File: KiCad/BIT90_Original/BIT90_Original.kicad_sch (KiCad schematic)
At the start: 0 parts

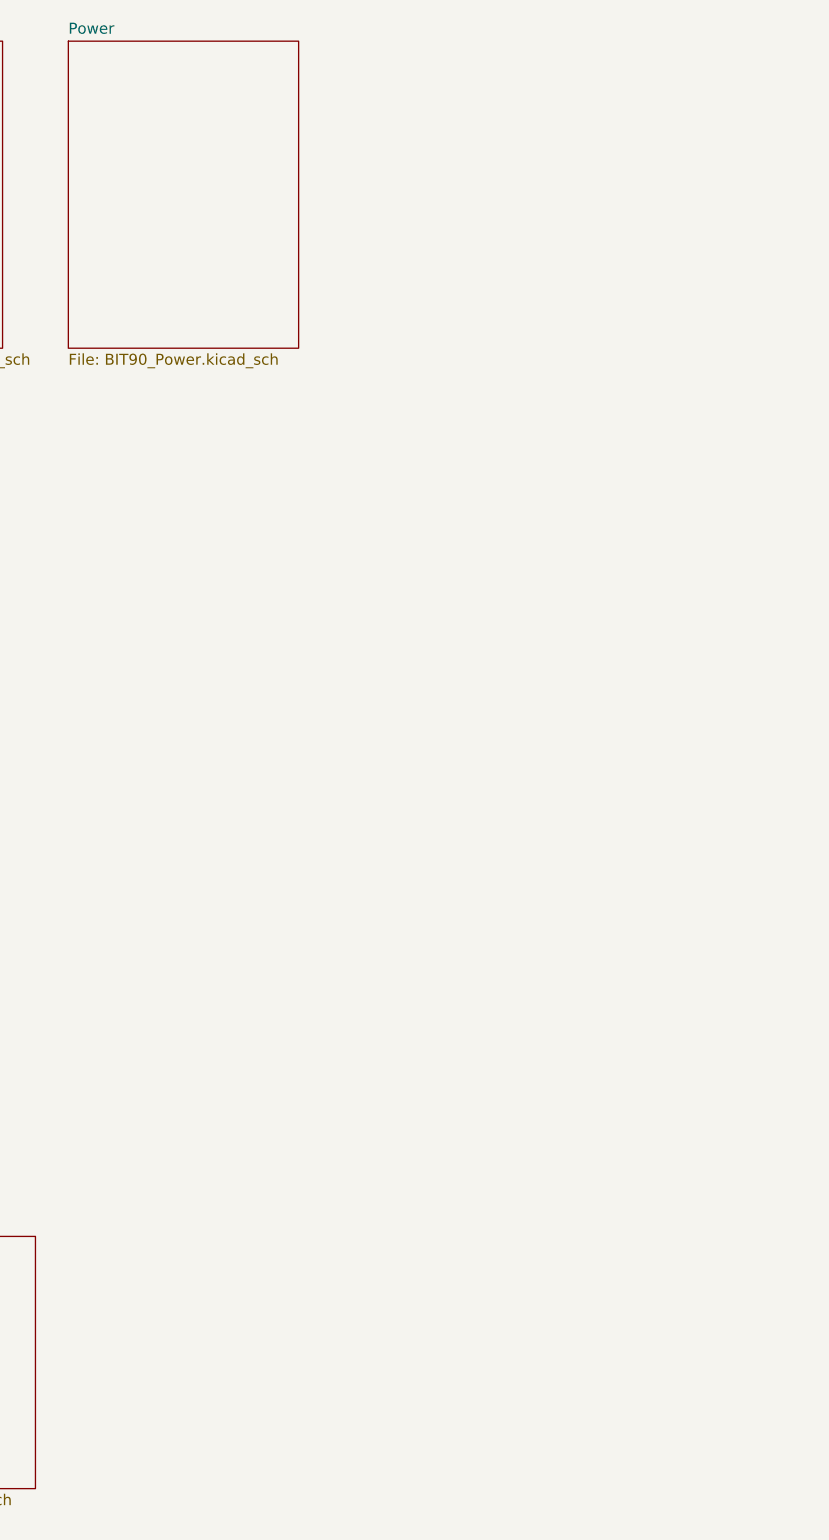
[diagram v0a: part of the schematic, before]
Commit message: Added "Processor" Sheet 6-1
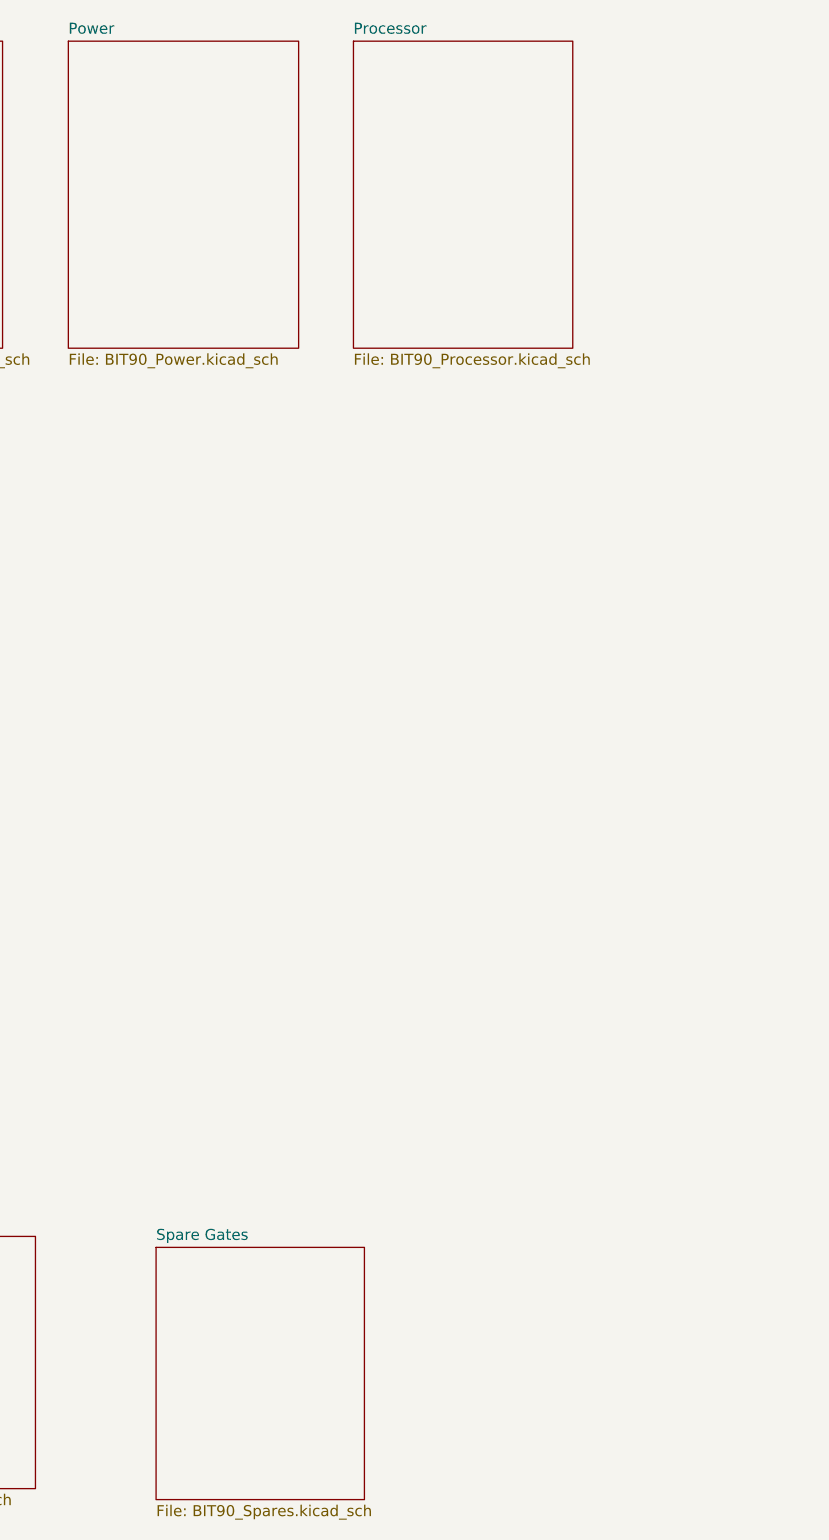
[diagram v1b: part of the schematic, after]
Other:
- added sheet Processor (BIT90_Processor.kicad_sch)
- added sheet Spare Gates (BIT90_Spares.kicad_sch)
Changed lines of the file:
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@@
+	)
+	(sheet
+		(at 88.9 21.59)
+		(size 25.4 35.56)
+		(exclude_from_sim no)
+		(in_bom yes)
+		(on_board yes)
+		(dnp no)
+		(fields_autoplaced yes)
+		(stroke
+			(width 0.1524)
+			(type solid)
+		)
+		(fill
+			(color 0 0 0 0.0000)
+		)
+		(property "Sheetname" "Processor"
+			(at 88.9 20.8784 0)
+			(effects
+				(font
+					(size 1.27 1.27)
+				)
+				(justify left bottom)
+			)
+		)
+		(property "Sheetfile" "BIT90_Processor.kicad_sch"
+			(at 88.9 57.7346 0)
+			(effects
+				(font
+					(size 1.27 1.27)
+				)
+				(justify left top)
+			)
+		)
+		(instances
+			(project "BIT90_Original"
+				(path "/d65498c3-6385-4920-ac0f-4c76daf90780"
+					(page "5")
+				)
+			)
+		)
 	)
 	(sheet
@@
 				)
 			)
+		)
+	)
+	(sheet
+		(at 66.04 161.29)
+		(size 24.13 29.21)
+		(exclude_from_sim no)
+		(in_bom yes)
+		(on_board yes)
+		(dnp no)
+		(fields_autoplaced yes)
+		(stroke
+			(width 0.1524)
+			(type solid)
+		)
+		(fill
+			(color 0 0 0 0.0000)
+		)
+		(property "Sheetname" "Spare Gates"
+			(at 66.04 160.5784 0)
+			(effects
+				(font
+					(size 1.27 1.27)
+				)
+				(justify left bottom)
+			)
+		)
+		(property "Sheetfile" "BIT90_Spares.kicad_sch"
+			(at 66.04 191.0846 0)
+			(effects
+				(font
+					(size 1.27 1.27)
+				)
+				(justify left top)
+			)
+		)
+		(instances
+			(project "BIT90_Original"
+				(path "/d65498c3-6385-4920-ac0f-4c76daf90780"
+					(page "6")
+				)
+			)

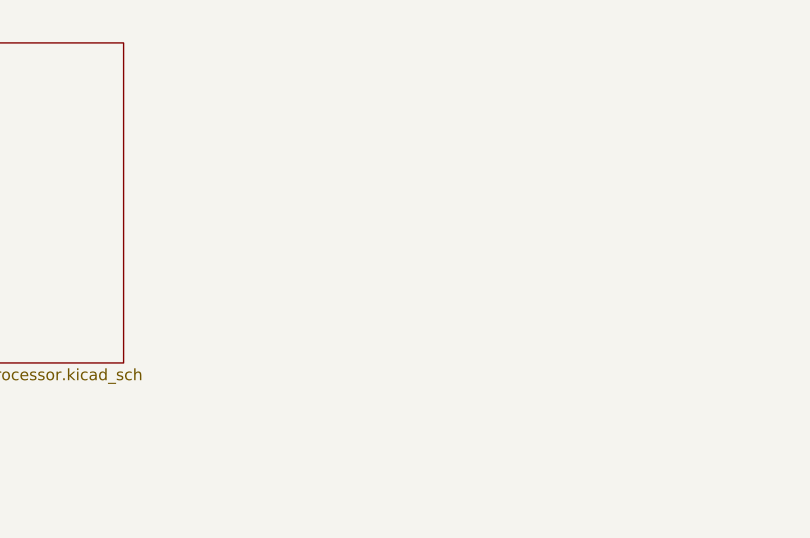
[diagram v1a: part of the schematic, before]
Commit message: Added "Video Control" schematic
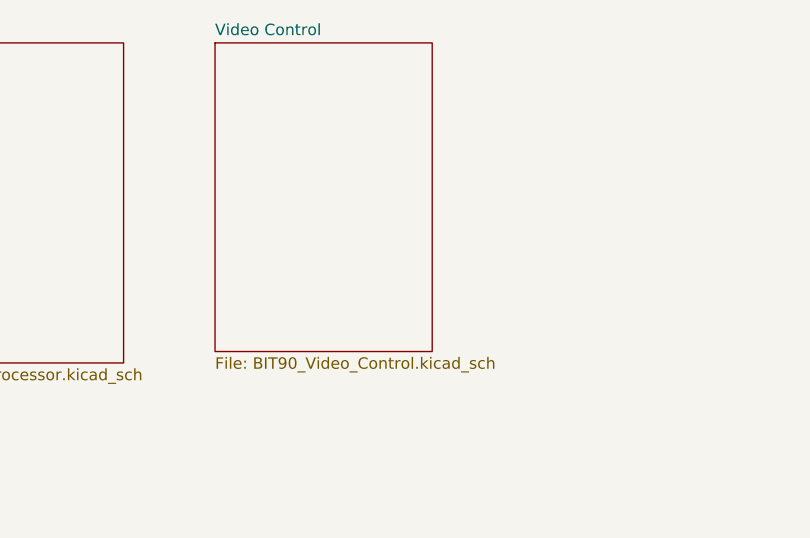
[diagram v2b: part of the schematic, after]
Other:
- added sheet Video Control (BIT90_Video_Control.kicad_sch)
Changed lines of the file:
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@@
+	)
+	(sheet
+		(at 124.46 21.59)
+		(size 24.13 34.29)
+		(exclude_from_sim no)
+		(in_bom yes)
+		(on_board yes)
+		(dnp no)
+		(fields_autoplaced yes)
+		(stroke
+			(width 0.1524)
+			(type solid)
+		)
+		(fill
+			(color 0 0 0 0.0000)
+		)
+		(property "Sheetname" "Video Control"
+			(at 124.46 20.8784 0)
+			(effects
+				(font
+					(size 1.27 1.27)
+				)
+				(justify left bottom)
+			)
+		)
+		(property "Sheetfile" "BIT90_Video_Control.kicad_sch"
+			(at 124.46 56.4646 0)
+			(effects
+				(font
+					(size 1.27 1.27)
+				)
+				(justify left top)
+			)
+		)
+		(instances
+			(project "BIT90_Original"
+				(path "/d65498c3-6385-4920-ac0f-4c76daf90780"
+					(page "7")
+				)
+			)
+		)
 	)
 	(sheet

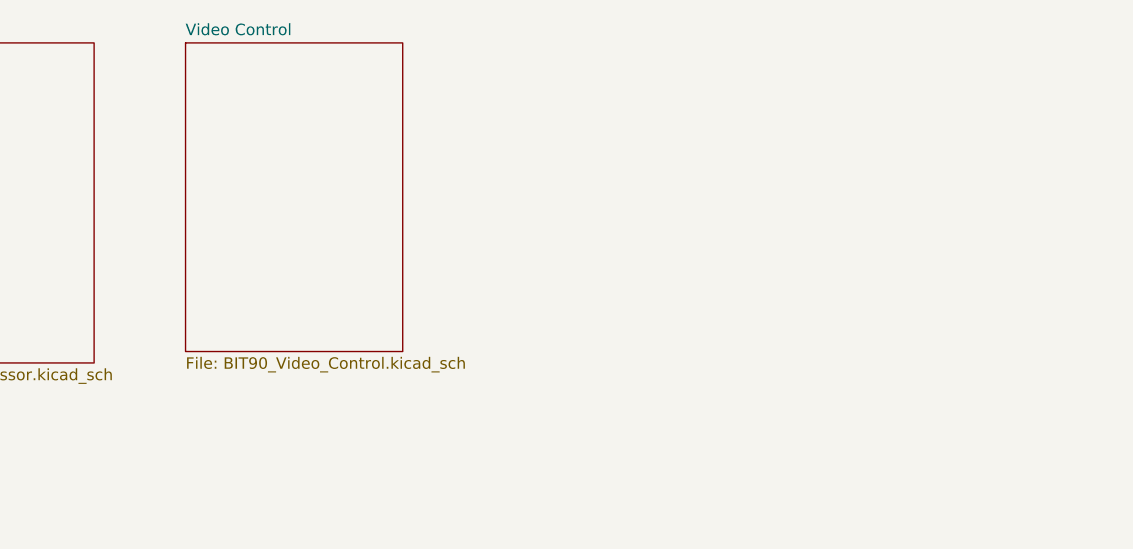
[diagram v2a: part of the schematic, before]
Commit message: Added "Joystick, Audio, Tape Out" schematic
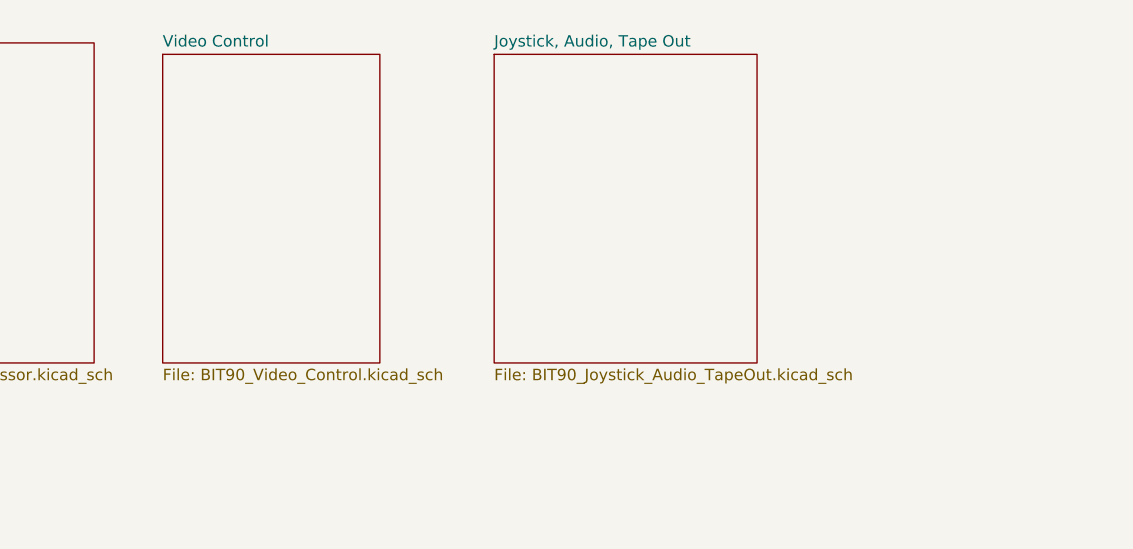
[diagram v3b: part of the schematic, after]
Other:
- added sheet Joystick, Audio, Tape Out (BIT90_Joystick_Audio_TapeOut.kicad_sch)
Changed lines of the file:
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@@
+	)
+	(sheet
+		(at 158.75 22.86)
+		(size 29.21 34.29)
+		(exclude_from_sim no)
+		(in_bom yes)
+		(on_board yes)
+		(dnp no)
+		(fields_autoplaced yes)
+		(stroke
+			(width 0.1524)
+			(type solid)
+		)
+		(fill
+			(color 0 0 0 0.0000)
+		)
+		(property "Sheetname" "Joystick, Audio, Tape Out"
+			(at 158.75 22.1484 0)
+			(effects
+				(font
+					(size 1.27 1.27)
+				)
+				(justify left bottom)
+			)
+		)
+		(property "Sheetfile" "BIT90_Joystick_Audio_TapeOut.kicad_sch"
+			(at 158.75 57.7346 0)
+			(effects
+				(font
+					(size 1.27 1.27)
+				)
+				(justify left top)
+			)
+		)
+		(instances
+			(project "BIT90_Original"
+				(path "/d65498c3-6385-4920-ac0f-4c76daf90780"
+					(page "8")
+				)
+			)
+		)
 	)
 	(sheet
@@
 	)
 	(sheet
-		(at 124.46 21.59)
+		(at 121.92 22.86)
 		(size 24.13 34.29)
 		(exclude_from_sim no)
@@
 		)
 		(property "Sheetname" "Video Control"
-			(at 124.46 20.8784 0)
+			(at 121.92 22.1484 0)
 			(effects
 				(font
@@
 		)
 		(property "Sheetfile" "BIT90_Video_Control.kicad_sch"
-			(at 124.46 56.4646 0)
+			(at 121.92 57.7346 0)
 			(effects
 				(font

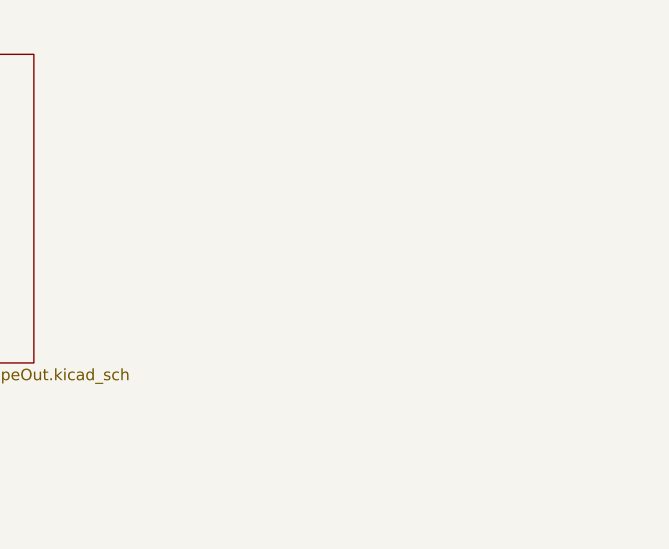
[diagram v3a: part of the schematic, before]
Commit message: Minor schematic corrections
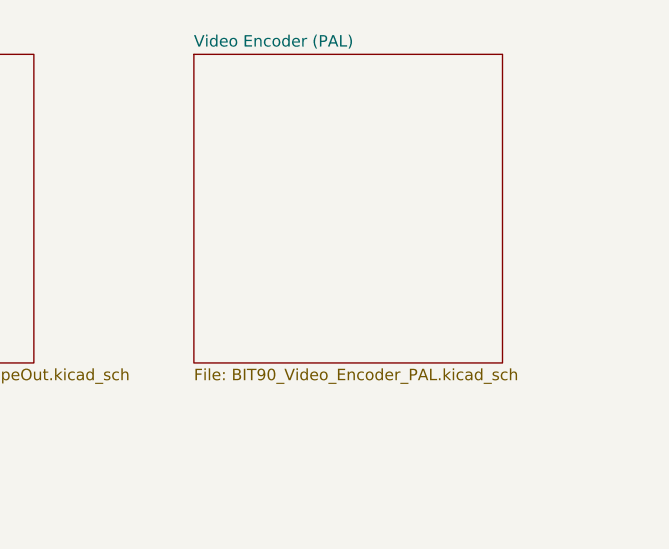
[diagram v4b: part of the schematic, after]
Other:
- added sheet Video Encoder (PAL) (BIT90_Video_Encoder_PAL.kicad_sch)
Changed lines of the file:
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@@
 		(rev "WIP")
 		(company "Brett Hallen")
-		(comment 4 "Based on original schematics from BIT Corporation")
+		(comment 4 "Based on original schematics from BIT Corporation (普澤有限公司)")
 	)
 	(text ">> WORK IN PROGRESS <<"
@@
 				)
 			)
+		)
+	)
+	(sheet
+		(at 205.74 22.86)
+		(size 34.29 34.29)
+		(exclude_from_sim no)
+		(in_bom yes)
+		(on_board yes)
+		(dnp no)
+		(fields_autoplaced yes)
+		(stroke
+			(width 0.1524)
+			(type solid)
+		)
+		(fill
+			(color 0 0 0 0.0000)
+		)
+		(property "Sheetname" "Video Encoder (PAL)"
+			(at 205.74 22.1484 0)
+			(effects
+				(font
+					(size 1.27 1.27)
+				)
+				(justify left bottom)
+			)
+		)
+		(property "Sheetfile" "BIT90_Video_Encoder_PAL.kicad_sch"
+			(at 205.74 57.7346 0)
+			(effects
+				(font
+					(size 1.27 1.27)
+				)
+				(justify left top)
+			)
+		)
+		(instances
+			(project "BIT90_Original"
+				(path "/d65498c3-6385-4920-ac0f-4c76daf90780"
+					(page "9")
+				)
+			)

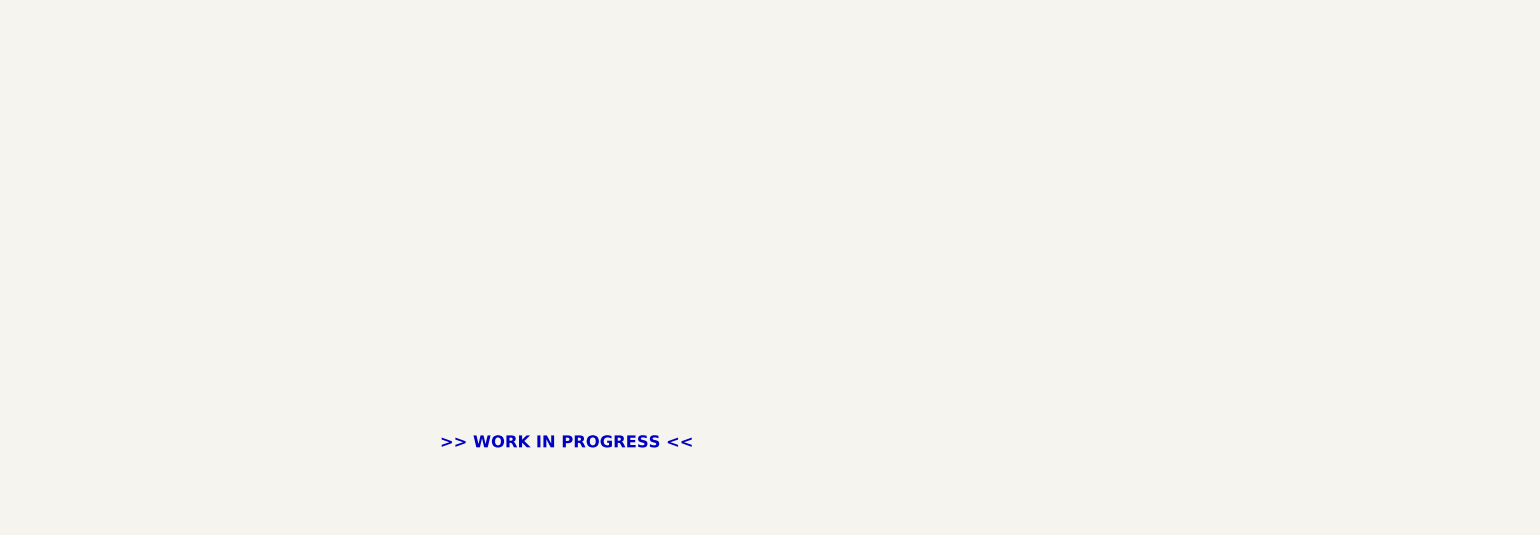
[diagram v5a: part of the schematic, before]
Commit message: Small updates/corrections
Managed to figure out some more errors/missing info from ColecoVision schematics & Henk's BIT90 motherboard underside photo
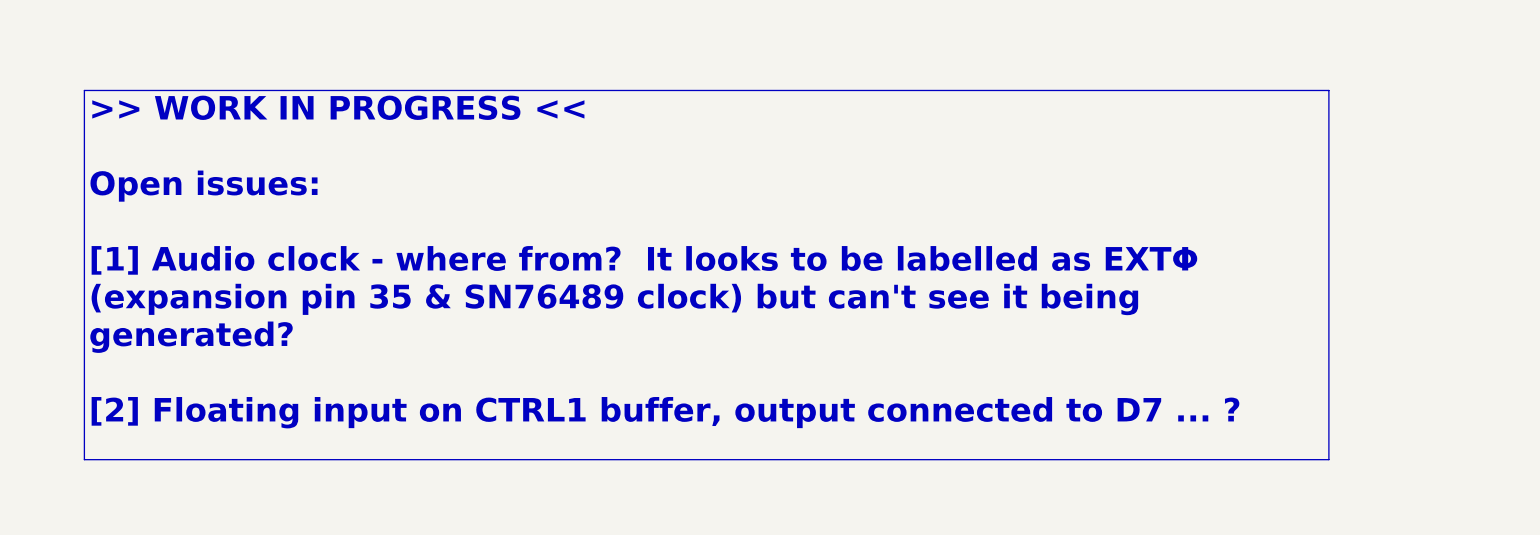
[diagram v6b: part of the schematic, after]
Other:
- note removed: ">> WORK IN PROGRESS <<"
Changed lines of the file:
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@@
 	(title_block
 		(title "BIT90 (PAL) Computer")
-		(date "3/JUN/2026")
+		(date "5/JUN/2026")
 		(rev "A")
 		(company "Brett Hallen")
 		(comment 4 "Based on original schematics from BIT Corporation (普澤有限公司)")
 	)
-	(text ">> WORK IN PROGRESS <<"
+	(text_box ">> WORK IN PROGRESS <<\n\nOpen issues:\n\n[1] Audio clock - where from?  It looks to be labelled as EXTΦ (expansion pin 35 & SN76489 clock) but can't see it being generated?\n\n[2] Floating input on CTRL1 buffer, output connected to D7 ... ?"
 		(exclude_from_sim no)
-		(at 224.79 175.514 0)
+		(at 121.92 100.33 0)
+		(size 265.43 78.74)
+		(margins 0.9525 0.9525 0.9525 0.9525)
+		(stroke
+			(width 0)
+			(type solid)
+		)
+		(fill
+			(type none)
+		)
 		(effects
 			(font
-				(size 2.54 2.54)
-				(thickness 0.508)
+				(size 5 5)
+				(thickness 1)
 				(bold yes)
 			)
+			(justify left top)
 		)
 	)
